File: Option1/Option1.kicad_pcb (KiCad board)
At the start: 2 copper layers, 86 x 62 mm, 0 parts

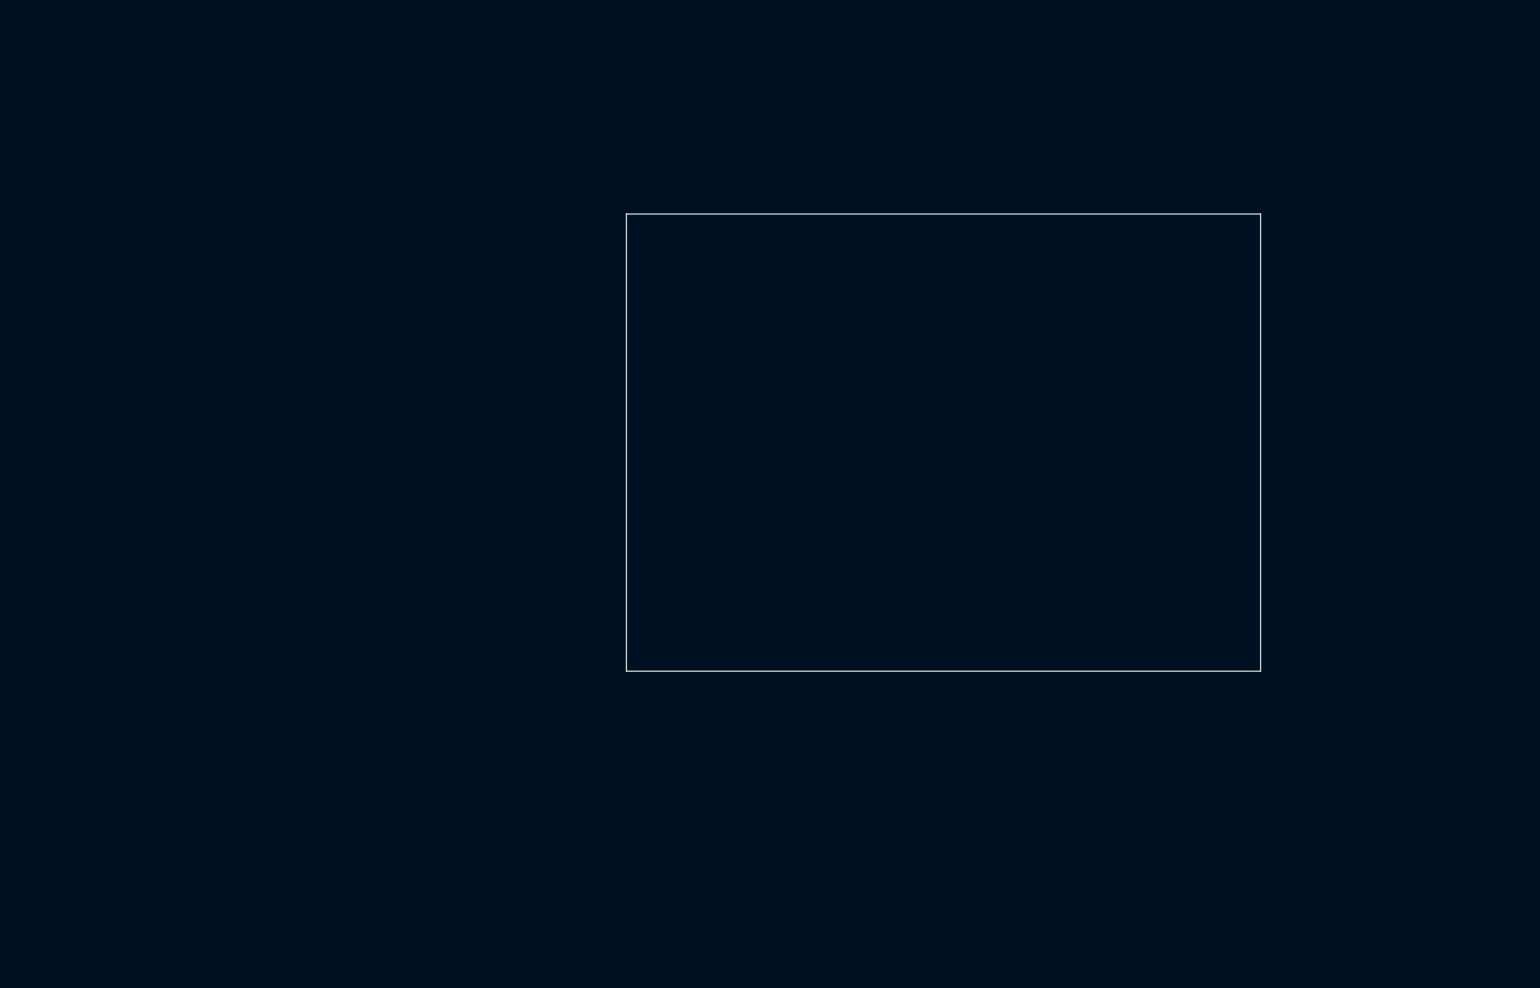
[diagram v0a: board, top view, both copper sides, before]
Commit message: Layout für Powersupply, CAN und Stecker hinzugefügt
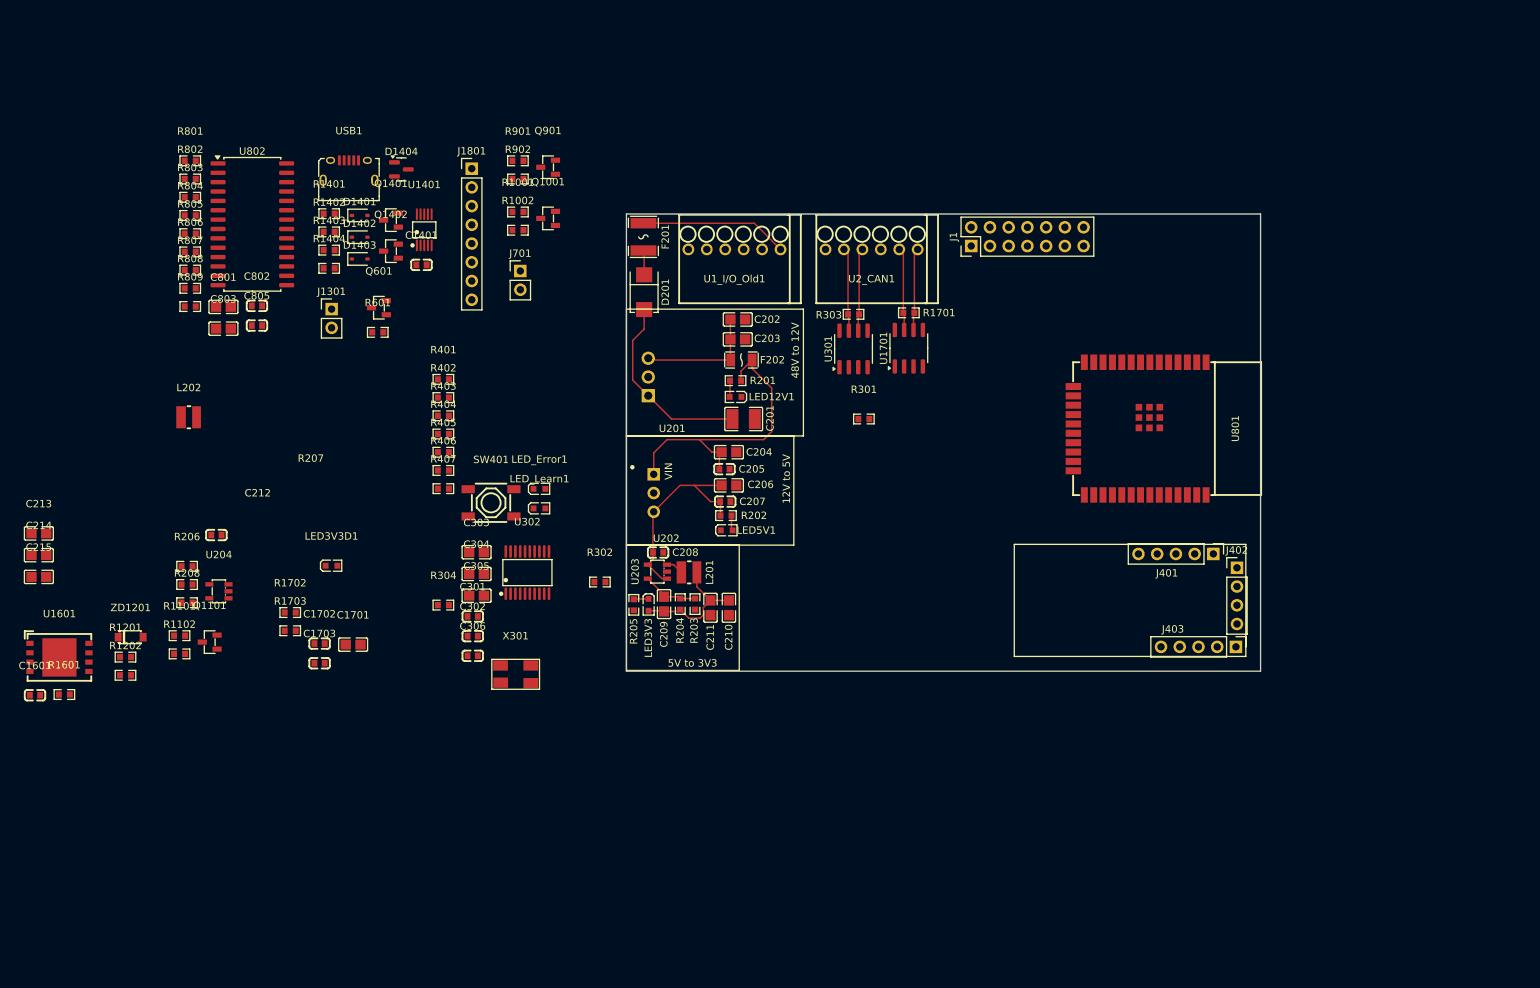
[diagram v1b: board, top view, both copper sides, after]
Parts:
- added C1401: 100nF, easyeda2kicad:C0603, F.Cu at (72.2, 56.9)
- added C1601: 100nF, easyeda2kicad:C0603, F.Cu at (19.8, 115.3)
- added C1701: 4.7nF, easyeda2kicad:C0805, F.Cu at (62.9, 108.4)
- added C1702: 100nF, easyeda2kicad:C0603, F.Cu at (58.4, 108.3)
- added C1703: 100nF, easyeda2kicad:C0603, F.Cu at (58.4, 110.9)
- added C201: 10uF / 63V, easyeda2kicad:C1210, F.Cu at (115.9, 77.8)
- added C202: 10uF / 16V, easyeda2kicad:C0805, F.Cu at (115.1, 64.3)
- added C203: 10uF / 16V, easyeda2kicad:C0805, F.Cu at (115.1, 67.0)
- added C204: 10uF / 25V, easyeda2kicad:C0805, F.Cu at (113.9, 82.3)
- added C205: 100nF / 25V, easyeda2kicad:C0603, F.Cu at (113.3, 84.6)
- added C206: 10uF / 25V, easyeda2kicad:C0805, F.Cu at (113.9, 86.8)
- added C207: 100nF / 25V, easyeda2kicad:C0603, F.Cu at (113.4, 89.0)
- added C208: 22uF / 6.3V, easyeda2kicad:C0603, F.Cu at (104.3, 95.9)
- added C209: 22pF, easyeda2kicad:C0805, F.Cu at (105.1, 102.9)
- added C210: 22uF, easyeda2kicad:C0805, F.Cu at (113.9, 103.4)
- added C211: 22uF, easyeda2kicad:C0805, F.Cu at (111.4, 103.4)
- added C212: 22uF / 6.3V, easyeda2kicad:C0603, F.Cu at (44.4, 93.5)
- added C213: 22pF, easyeda2kicad:C0805, F.Cu at (20.3, 93.3)
- added C214: 22uF, easyeda2kicad:C0805, F.Cu at (20.3, 96.3)
- added C215: 22uF, easyeda2kicad:C0805, F.Cu at (20.3, 99.2)
- added C301: 100nF, easyeda2kicad:C0603, F.Cu at (79.2, 104.6)
- added C302: 100nF, easyeda2kicad:C0603, F.Cu at (79.2, 107.2)
- added C303: 4.7nF, easyeda2kicad:C0805, F.Cu at (79.7, 95.9)
- added C304: 22pF, easyeda2kicad:C0805, F.Cu at (79.7, 98.8)
- added C305: 22pF, easyeda2kicad:C0805, F.Cu at (79.7, 101.8)
- added C306: 100nF, easyeda2kicad:C0603, F.Cu at (79.2, 109.9)
- added C801: 22uF, easyeda2kicad:C0805, F.Cu at (45.3, 62.6)
- added C802: 100nF, easyeda2kicad:C0603, F.Cu at (49.9, 62.5)
- added C803: 10 uF, easyeda2kicad:C0805, F.Cu at (45.3, 65.5)
- added C805: 100nF, easyeda2kicad:C0603, F.Cu at (49.9, 65.1)
- added D1401: 1N5819WS, Diode_SMD:D_SOD-323, F.Cu at (63.8, 50.2)
- added D1402: 1N5819WS, Diode_SMD:D_SOD-323, F.Cu at (63.8, 53.1)
- added D1403: 1N5819WS, Diode_SMD:D_SOD-323, F.Cu at (63.8, 56.1)
- added D1404: BAT54C, Package_TO_SOT_SMD:SOT-23, F.Cu at (69.5, 44.0)
- added D201: SS310_C14281, easyeda2kicad:SMB_L4.6-W3.6-LS5.3-RD, F.Cu at (102.4, 60.6)
- added F201: JK-MSMD020-60V, easyeda2kicad:F1812, F.Cu at (102.3, 53.1)
- added F202: JK-NSMD075-13.2, easyeda2kicad:F1206, F.Cu at (115.6, 69.8)
- added J1: Conn_02x07_Odd_Even, Connector_PinHeader_2.54mm:PinHeader_2x07_P2.54mm_Vertical, F.Cu at (146.8, 54.3)
- added J1301: Conn_01x02_Socket, Connector_PinHeader_2.54mm:PinHeader_1x02_P2.54mm_Vertical, F.Cu at (60.0, 62.9)
- added J1801: Conn_01x08_Socket, Connector_PinHeader_2.54mm:PinHeader_1x08_P2.54mm_Vertical, F.Cu at (79.0, 43.8)
- added J401: Conn_01x05_Pin, Connector_PinHeader_2.54mm:PinHeader_1x05_P2.54mm_Vertical, F.Cu at (179.6, 96.1)
- added J402: Conn_01x04_Pin, Connector_PinHeader_2.54mm:PinHeader_1x04_P2.54mm_Vertical, F.Cu at (182.8, 98.0)
- added J403: Conn_01x05_Pin, Connector_PinHeader_2.54mm:PinHeader_1x05_P2.54mm_Vertical, F.Cu at (182.7, 108.7)
- added J701: Conn_01x02_Socket, Connector_PinHeader_2.54mm:PinHeader_1x02_P2.54mm_Vertical, F.Cu at (85.6, 57.7)
- added L201: 2.2uH, easyeda2kicad:IND-SMD_L3.0-W3.0_NR3010, F.Cu at (108.5, 98.6)
- added L202: 2.2uH, easyeda2kicad:IND-SMD_L3.0-W3.0_NR3010, F.Cu at (40.6, 77.6)
- added LED12V1: XL-1608SYGC-06, easyeda2kicad:LED0603-RD_GREEN, F.Cu at (114.8, 74.8)
- added LED3V3: XL-1608SYGC-06, easyeda2kicad:LED0603-RD_GREEN, F.Cu at (103.0, 103.0)
- added LED3V3D1: XL-1608SYGC-06, easyeda2kicad:LED0603-RD_GREEN, F.Cu at (60.0, 97.7)
- added LED5V1: XL-1608SYGC-06, easyeda2kicad:LED0603-RD_GREEN, F.Cu at (113.6, 92.9)
- added LED_Error1: XL-1608SYGC-06, easyeda2kicad:LED0603-RD_GREEN, F.Cu at (88.2, 87.3)
- added LED_Learn1: XL-1608SYGC-06, easyeda2kicad:LED0603-RD_GREEN, F.Cu at (88.2, 89.9)
- added Q1001: JY2302, easyeda2kicad:SOT-23-3_L2.9-W1.3-P0.95-LS2.4-BR, F.Cu at (89.4, 50.6)
- added Q1101: JY2302, easyeda2kicad:SOT-23-3_L2.9-W1.3-P0.95-LS2.4-BR, F.Cu at (43.5, 108.1)
- added Q1401: BC817-40, easyeda2kicad:SOT-23-3_L2.9-W1.3-P1.90-LS2.4-BR, F.Cu at (68.1, 50.8)
- added Q1402: BC817-40, easyeda2kicad:SOT-23-3_L2.9-W1.3-P1.90-LS2.4-BR, F.Cu at (68.1, 55.0)
- added Q601: JY2302, easyeda2kicad:SOT-23-3_L2.9-W1.3-P0.95-LS2.4-BR, F.Cu at (66.4, 62.7)
- added Q901: JY2302, easyeda2kicad:SOT-23-3_L2.9-W1.3-P0.95-LS2.4-BR, F.Cu at (89.4, 43.7)
- added R1001: 1k, easyeda2kicad:R0603, F.Cu at (85.3, 49.7)
- added R1002: 10k, easyeda2kicad:R0603, F.Cu at (85.3, 52.2)
- added R1101: 1k, easyeda2kicad:R0603, F.Cu at (39.4, 107.2)
- added R1102: 10k, easyeda2kicad:R0603, F.Cu at (39.4, 109.7)
- added R1201: 27k, easyeda2kicad:R0603, F.Cu at (32.1, 110.1)
- added R1202: 10k, easyeda2kicad:R0603, F.Cu at (32.1, 112.6)
- added R1401: 500Ω, easyeda2kicad:R0603, F.Cu at (59.7, 50.0)
- added R1402: 2k2, easyeda2kicad:R0603, F.Cu at (59.7, 52.4)
- added R1403: 4k7, easyeda2kicad:R0603, F.Cu at (59.7, 54.9)
- added R1404: 2k2, easyeda2kicad:R0603, F.Cu at (59.7, 57.4)
- added R1601: 10k, easyeda2kicad:R0603, F.Cu at (23.8, 115.2)
- added R1701: 120Ω, easyeda2kicad:R0603, F.Cu at (138.3, 63.4)
- added R1702: 33k, easyeda2kicad:R0603, F.Cu at (54.4, 104.0)
- added R1703: 33k, easyeda2kicad:R0603, F.Cu at (54.4, 106.5)
- added R201: 1.8kΩ, easyeda2kicad:R0603, F.Cu at (114.8, 72.6)
- added R202: 560Ω, easyeda2kicad:R0603, F.Cu at (113.5, 90.9)
- added R203: 49.9k, easyeda2kicad:R0603, F.Cu at (109.3, 102.9)
- added R204: 220k, easyeda2kicad:R0603, F.Cu at (107.3, 102.9)
- added R205: 220Ω, easyeda2kicad:R0603, F.Cu at (101.0, 103.0)
- added R206: 49.9k, easyeda2kicad:R0603, F.Cu at (40.4, 97.8)
- added R207: 220k, easyeda2kicad:R0603, F.Cu at (40.4, 100.2)
- added R208: 220Ω, easyeda2kicad:R0603, F.Cu at (40.4, 102.7)
- added R301: 33k, easyeda2kicad:R0603, F.Cu at (132.2, 77.8)
- added R302: 33k, easyeda2kicad:R0603, F.Cu at (96.4, 99.9)
- added R303: 120Ω, easyeda2kicad:R0603, F.Cu at (130.8, 63.6)
- added R304: 10kΩ, easyeda2kicad:R0603, F.Cu at (75.2, 103.0)
- added R401: 220Ω, easyeda2kicad:R0603, F.Cu at (75.2, 72.4)
- added R402: 10K, easyeda2kicad:R0603, F.Cu at (75.2, 74.9)
- added R403: 10k, easyeda2kicad:R0603, F.Cu at (75.2, 77.4)
- added R404: 10k, easyeda2kicad:R0603, F.Cu at (75.2, 79.8)
- added R405: 10k, easyeda2kicad:R0603, F.Cu at (75.2, 82.3)
- added R406: 220Ω, easyeda2kicad:R0603, F.Cu at (75.2, 84.8)
- added R407: 10K, easyeda2kicad:R0603, F.Cu at (75.2, 87.2)
- added R601: 1k, easyeda2kicad:R0603, F.Cu at (66.3, 66.0)
- added R801: 10kΩ, easyeda2kicad:R0603, F.Cu at (40.8, 42.8)
- added R802: 10kΩ, easyeda2kicad:R0603, F.Cu at (40.8, 45.3)
- added R803: 10kΩ, easyeda2kicad:R0603, F.Cu at (40.8, 47.7)
- added R804: 10kΩ, easyeda2kicad:R0603, F.Cu at (40.8, 50.2)
- added R805: 10kΩ, easyeda2kicad:R0603, F.Cu at (40.8, 52.7)
- added R806: 4.7kΩ, easyeda2kicad:R0603, F.Cu at (40.8, 55.1)
- added R807: 4.7kΩ, easyeda2kicad:R0603, F.Cu at (40.8, 57.6)
- added R808: 10kΩ, easyeda2kicad:R0603, F.Cu at (40.8, 60.1)
- added R809: 10k, easyeda2kicad:R0603, F.Cu at (40.8, 62.5)
- added R901: 1k, easyeda2kicad:R0603, F.Cu at (85.3, 42.8)
- added R902: 10k, easyeda2kicad:R0603, F.Cu at (85.3, 45.3)
- added SW401: 4*4*1.7, easyeda2kicad:SW-SMD_4P-L5.2-W5.2-P3.70-LS6.5, F.Cu at (81.6, 89.2)
- added U1401: CH340X, easyeda2kicad:MSOP-10_L3.0-W3.0-P0.50-LS5.0-BL, F.Cu at (72.6, 52.1)
- added U1601: W25Q512JVEIQ, easyeda2kicad:WSON-8_L8.0-W6.0-P1.27-TL-EP, F.Cu at (23.1, 110.1)
- added U1701: TJA1051T-3, Package_SO:SOIC-8_3.9x4.9mm_P1.27mm, F.Cu at (138.3, 68.2)
- added U1_I/O_Old1: 1989780, easyeda2kicad:CONN-TH_6P-P2.50_1989780, F.Cu at (114.7, 54.8)
- added U201: U7812-500, easyeda2kicad:PWRM-TH_3P-L11.6-W9.0-P2.54, F.Cu at (103.0, 72.1)
- added U202: K7805-500R2_C909663, easyeda2kicad:PWRM-TH_K78XX-500R3, F.Cu at (103.7, 87.8)
- added U203: SY8089AAAC, easyeda2kicad:SOT-23-5_L3.0-W1.7-P0.95-LS2.8-BR, F.Cu at (104.2, 98.5)
- added U204: SY8089AAAC, easyeda2kicad:SOT-23-5_L3.0-W1.7-P0.95-LS2.8-BR, F.Cu at (44.7, 101.2)
- added U2_CAN1: 1989780, easyeda2kicad:CONN-TH_6P-P2.50_1989780, F.Cu at (133.2, 54.8)
- added U301: TJA1051T-3, Package_SO:SOIC-8_3.9x4.9mm_P1.27mm, F.Cu at (130.8, 68.3)
- added U302: MCP2515-I/ST, easyeda2kicad:TSSOP-20_L6.5-W4.4-P0.65-LS6.4-BL, F.Cu at (86.6, 98.6)
- added U801: ESP32-WROOM-32E-N4, easyeda2kicad:WIFI-SMD_ESP32-WROOM-32E-A, F.Cu at (169.6, 79.1)
- added U802: MCP23017_SO, Package_SO:SOIC-28W_7.5x17.9mm_P1.27mm, F.Cu at (49.3, 51.4)
- added USB1: 10118194-0001LF, easyeda2kicad:MICRO-USB-SMD_10118194-0001LF, F.Cu at (62.4, 44.1)
- added X301: XL1EL89CSI-111YLC-8M, easyeda2kicad:CRYSTAL-SMD_4P-L5.0-W3.2-BL-7I12288F20UCG, F.Cu at (85.0, 112.4)
- added ZD1201: BZT52C3V6_C2113, easyeda2kicad:SOD-123_L2.8-W1.8-LS3.7-RD, F.Cu at (32.8, 107.4)
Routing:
- net 12V: track 0.00 -> 40.4 mm
- net 5V: track 0.00 -> 27.9 mm
- net /Powersupply/48V_FUSED: track 0.00 -> 25.9 mm
- net 48V: track 0.00 -> 20.1 mm
- net 3.3V: track 0.00 -> 17.7 mm
- net /Powersupply/12V_OUT: track 0.00 -> 16.8 mm
- net /CAN2_Tranciever/CAN_H: track 0.00 -> 11.3 mm
- net /CAN2_Tranciever/CAN_L: track 0.00 -> 11.3 mm
- net /CAN1 Tranciever/CAN_H: track 0.00 -> 11.2 mm
- net /CAN1 Tranciever/CAN_L: track 0.00 -> 11.2 mm
- net Net-(U203-FB): track 0.00 -> 7.66 mm
- net Net-(D201-A): track 0.00 -> 3.33 mm
- net Net-(U203-LX): track 0.00 -> 2.38 mm
- net Net-(LED12V1-A): track 0.00 -> 2.22 mm
- net Net-(LED5V1-A): track 0.00 -> 2.06 mm
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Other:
- board text added: "12V to 5V"
- board text added: "48V to 12V"
- board text added: "5V to 3V3"
- board text added: "Maße und platzierung korrigeren"
- board text added: "SVS CX-12R"

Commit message: MCT und SPI zu Layout hinzugefügt
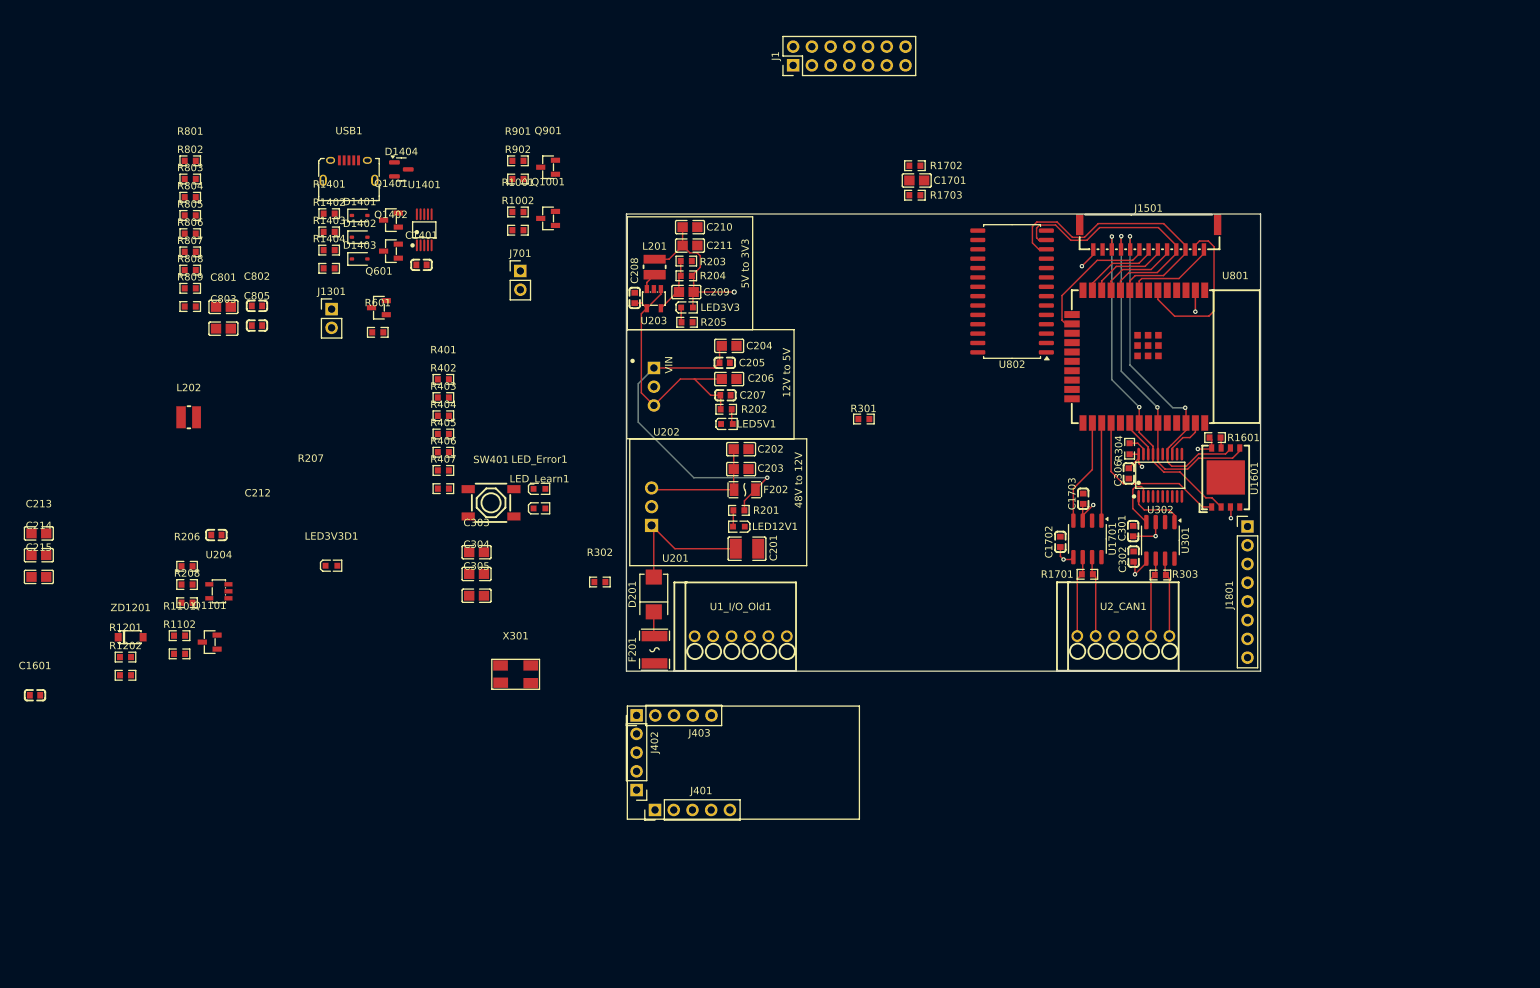
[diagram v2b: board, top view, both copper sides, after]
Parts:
- added J1501: GH-13AB, easyeda2kicad:CONN-SMD_GH-13AB, F.Cu at (170.8, 53.1)
- moved U1601 160.0 mm to (181.3, 85.7), turned to 90 degrees
- moved R1601 159.9 mm to (179.8, 80.3), turned to 180 degrees
- moved J1801 115.9 mm to (184.2, 92.4)
- moved C1703 105.9 mm to (161.9, 88.6), turned to 90 degrees
- moved R1702 104.2 mm to (139.1, 43.5)
- moved U802 103.4 mm to (152.3, 60.5), turned to 180 degrees
- moved R1703 103.3 mm to (139.1, 47.5)
- moved C1702 101.4 mm to (158.8, 94.5), turned to 90 degrees
- moved C1701 99.0 mm to (139.4, 45.5), turned to 180 degrees
- moved R304 95.5 mm to (168.2, 81.8), turned to -90 degrees
- moved C306 92.3 mm to (168.1, 85.2), turned to -90 degrees
- moved C301 90.3 mm to (168.7, 93.0), turned to 90 degrees
- moved C302 90.3 mm to (168.8, 96.5), turned to 90 degrees
- moved U302 86.8 mm to (172.4, 85.4)
- moved J402 86.8 mm to (101.4, 128.1), turned to 180 degrees
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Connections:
- net SCL renamed IO33
- J1801 pad 2: IO18 -> IO22
- J1801 pad 3: IO17 -> IO21
- Q901 pad 2: /Notaus Schalter/Notaus_VCU -> GND
- Q901 pad 3: GND -> /Notaus Schalter/Notaus_VCU
- R806 pad 1: SDA -> IO25
- U1601 pad 1: IO22 -> IO17
- U1601 pad 5: IO17 -> IO21
- U1601 pad 6: IO18 -> IO22
- U1701 pad 1: IO26 -> IO16
- U1701 pad 4: IO27 -> IO4
- U2_CAN1 pad 4: /CAN2_Tranciever/CAN_L -> unconnected-(U2_CAN1-Pad4)
- U2_CAN1 pad 5: /CAN2_Tranciever/CAN_H -> /CAN2_Tranciever/CAN_L
- U2_CAN1 pad 6: unconnected-(U2_CAN1-Pad6) -> /CAN2_Tranciever/CAN_H
- U302 pad 13: IO25 -> IO23
- U302 pad 14: IO18 -> IO22
- U302 pad 16: IO17 -> IO21
- U302 pad 18: IO23 -> IO18
- U801 pad 8: SDA -> IO32
- U802 pad 13: SDA -> IO25
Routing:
- net IO22: track 0.00 -> 47.5 mm, vias 0 -> 2
- net IO21: track 0.00 -> 47.0 mm, vias 0 -> 2
- net IO19: track 0.00 -> 46.4 mm, vias 0 -> 2
- net IO33: track 0.00 -> 39.8 mm
- net IO25: track 0.00 -> 35.9 mm
- net 3.3V: track 17.7 -> 47.5 mm, vias 0 -> 8
- net IO34: track 0.00 -> 22.5 mm
- net IO17: track 0.00 -> 22.2 mm
- net 48V: track 20.1 -> 0.00 mm
- net 5V: track 27.9 -> 46.7 mm, vias 0 -> 2
- net IO13: track 0.00 -> 18.3 mm
- net IO4: track 0.00 -> 14.3 mm
- net IO16: track 0.00 -> 13.3 mm
- net IO32: track 0.00 -> 12.1 mm
- net IO27: track 0.00 -> 11.0 mm
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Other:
- board text removed: "Maße und platzierung korrigeren"

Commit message: funkempfänger mit Beschaltung zu Layout hinzugefügt, SPI und I2C teilnehmer geroutet, Löcher hinzugefügt, Stecker platziert
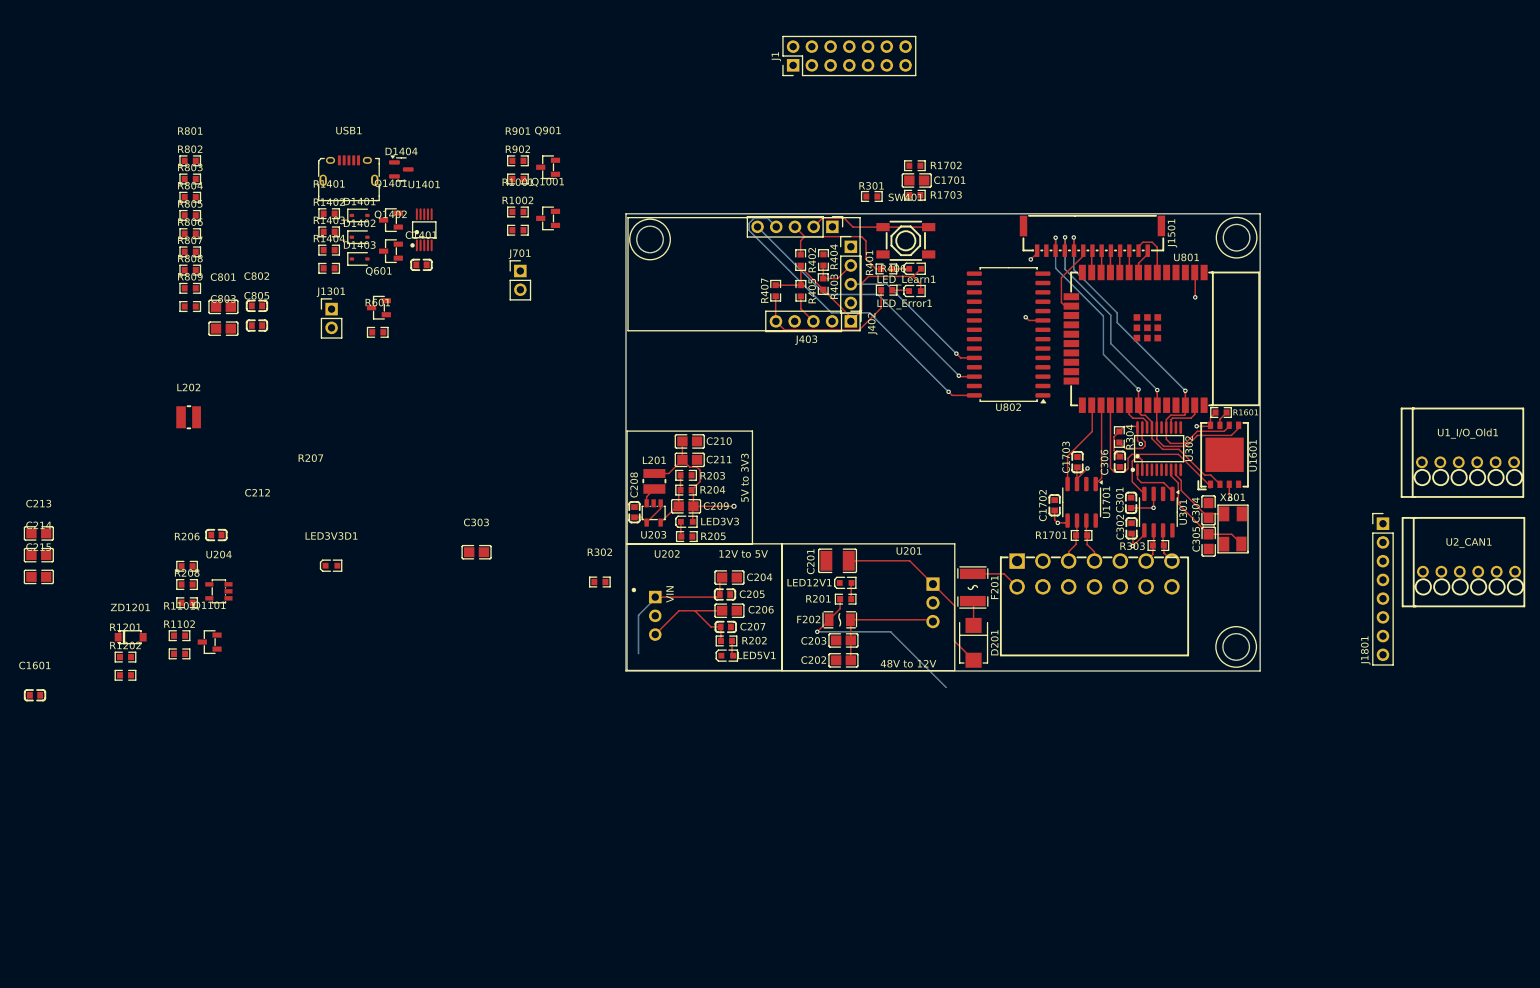
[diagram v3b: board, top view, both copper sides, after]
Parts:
- added J503: KF2EDGKRG-3.5-2*7P, easyeda2kicad:CONN-TH_14P-P3.50_KEFA_KF2EDGKRG-3.5-2X7P, F.Cu at (163.5, 98.8)
- moved U1_I/O_Old1 101.4 mm to (214.1, 83.7)
- moved C304 99.6 mm to (178.9, 90.2), turned to -90 degrees
- moved C305 99.6 mm to (179.0, 94.4), turned to 90 degrees
- moved X301 99.3 mm to (182.3, 92.7), turned to 90 degrees
- moved J401 82.7 mm to (127.9, 51.7), turned to -90 degrees
- moved J402 79.2 mm to (130.4, 54.4), turned to 0 degrees
- moved SW401 66.5 mm to (137.9, 53.6)
- moved R406 64.9 mm to (135.3, 60.3)
- moved R401 61.9 mm to (135.3, 57.5)
- moved J403 60.8 mm to (130.4, 64.6), turned to -90 degrees
- moved LED_Learn1 60.4 mm to (139.1, 57.4)
- moved LED_Error1 57.5 mm to (139.1, 60.5)
- moved R404 56.7 mm to (126.7, 56.2), turned to 90 degrees
- moved R403 54.5 mm to (126.7, 59.5), turned to -90 degrees
- moved R405 53.2 mm to (123.7, 60.4), turned to 90 degrees
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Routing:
- net RX_4: track 0.00 -> 45.2 mm, vias 0 -> 1
- net 3.3V: track 47.5 -> 86.8 mm, vias 8 -> 9
- net RX_3: track 0.00 -> 37.8 mm, vias 0 -> 1
- net IO33: track 39.8 -> 2.97 mm
- net IO25: track 35.9 -> 2.97 mm
- net Fehler_LED: track 0.00 -> 21.8 mm
- net RX_2: track 0.00 -> 20.9 mm, vias 0 -> 1
- net LED_Modus: track 0.00 -> 18.1 mm
- net Lernmodus: track 0.00 -> 16.6 mm
- net Net-(U302-OSC2): track 0.00 -> 15.8 mm
- net IO34: track 22.5 -> 7.04 mm
- net 5V: track 46.7 -> 32.0 mm
- net Net-(U302-OSC1): track 0.00 -> 10.7 mm
- net IO32: track 12.1 -> 3.48 mm
- net IO13: track 18.3 -> 9.81 mm
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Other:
- outline, holes or cut-outs redrawn
